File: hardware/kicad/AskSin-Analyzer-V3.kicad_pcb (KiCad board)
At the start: 4 copper layers, 118 x 46 mm, 38 parts, among them J1 Pi GPIO, J2 AVR-ISP-6, J5 OLED I2C, J6 Taster, J7 WS2812, U1 MCP1754S-3302xCB, U2 ATmega328P-AU, U3 E07-900M10S, Y1 8MHz

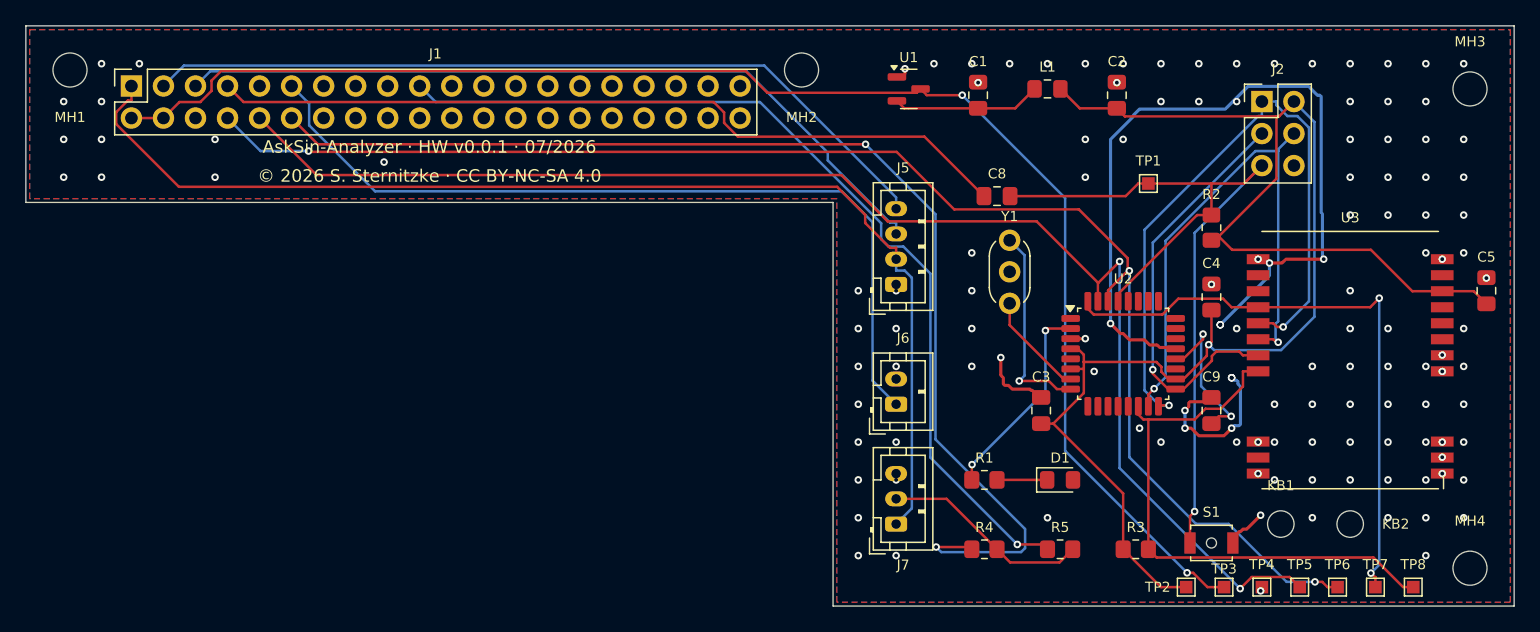
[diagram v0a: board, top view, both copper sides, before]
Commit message: Hardware v0.1.0: J1 korrigiert, Platine liegt jetzt neben dem Pi
Zwei Ursachen, ein Neuentwurf:

1. **J1 war gespiegelt.** Der Footprint wurde aus der offiziellen Vorlage
   RaspberryPi-HAT übernommen, aber ohne deren Flip auf die Unterseite.
   Die ungerade Pinreihe saß dadurch richtig, die gerade 2,54 mm auf der
   falschen Seite — aufgesteckt landet jedes Pad einen Pin daneben
   (5 V auf 3,3 V, Masse auf GPIOs). generate_pcb.py flippt J1 jetzt wie
   die Vorlage und prüft die vier Eckpads hart gegen das Pi-Raster; ein
   erneuter Fehler bricht den Lauf ab.

2. **Neue Bauform:** T-förmig statt L-förmig. Der Körper (88 × 34 mm)
   liegt parallel neben dem Pi an der Header-Seite und steht 20 mm nach
   hinten über (SD-Seite) — nicht mehr über den USB/Ethernet-Buchsen. Der
   Arm (65 × 8 mm) trägt nur die Buchse und die beiden HAT-Bohrungen.
   Funkmodul samt IPEX-Buchse sitzt im hinteren Überstand, die
   Peripheriestecker an der Frontkante.

Routing-Kette an die neue Geometrie angepasst und robuster gemacht:
- Masseflächen nur noch auf den Innenlagen; jedes SMD-Massepad bekommt
  vor dem Routen sein Stützvia (geometrisch auf Freiraum geprüft), GND
  bleibt aus dem Autorouter heraus. Damit entfallen die Splitterinseln
  und verhungerten Thermal-Speichen der Außenlagen-Füllung.
- Bohrloch-zu-Bohrloch-Wächter (räumlich indiziert) im eigenen Router
- offene Reste von Freerouting werden per A* nachgeroutet, doppelte Vias
  entfernt, alle Vias getentet
- Platinenmarkierung sucht sich ihren freien Platz selbst
- rebuild.py: baut so lange neu, bis DRC 0/0, Netzliste exakt und alle
  Massepads angebunden sind (Freerouting streut)
- finish_board.py: Absturz beim Entfernen alter Markierungstexte behoben
  (Remove -> Delete), Aufruf nie definierter Helfer entfernt

Prüfstand: ERC 0/0, DRC 0 Fehler / 0 Warnungen / 0 unverbunden,
Netzliste exakt gegen die Spezifikation, J1 gegen die HAT-Vorlage.

Co-Authored-By: Claude Fable 5 <noreply@anthropic.com>
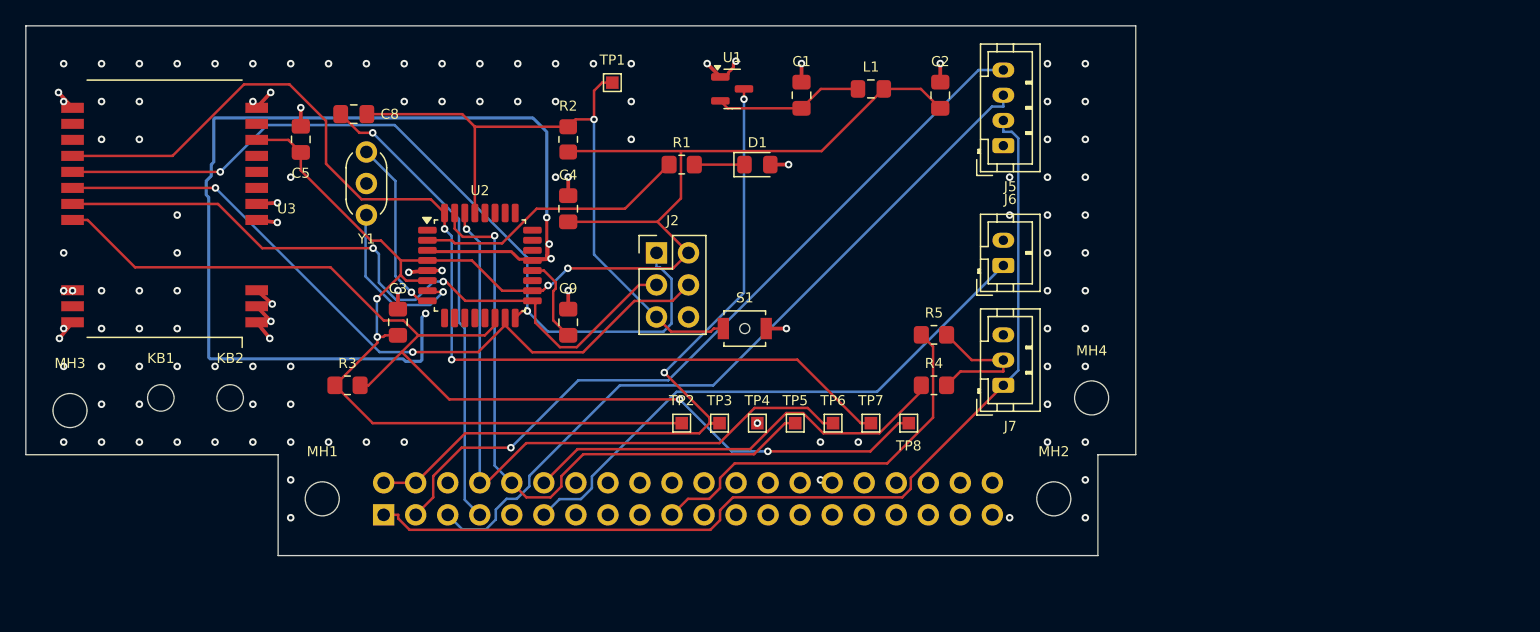
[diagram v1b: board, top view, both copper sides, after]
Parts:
- J1: moved to B.Cu
- R4: value 390 -> 390 DNP
- R5: value 0R DNP -> 0R
- moved MH3 113.9 mm to (103.5, 90.5)
- moved C5 94.8 mm to (121.8, 69.0)
- moved U3 94.8 mm to (111.0, 74.5)
- moved KB1 89.4 mm to (110.7, 89.5)
- moved KB2 89.4 mm to (116.2, 89.5)
- moved R3 63.8 mm to (125.5, 88.5)
- moved C3 51.5 mm to (129.5, 83.5)
- moved C4 51.5 mm to (143.0, 74.5)
- moved C9 51.5 mm to (143.0, 83.5)
- moved R2 51.5 mm to (143.0, 69.0)
- moved U2 51.5 mm to (136.0, 79.0)
- moved Y1 51.5 mm to (127.0, 75.0)
- moved C8 51.4 mm to (126.0, 67.0)
- moved J2 49.5 mm to (150.0, 78.0)
- moved TP1 43.2 mm to (146.5, 64.5)
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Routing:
- net UART_PI_TX: track 115.7 -> 52.9 mm, vias 3 -> 1
- net UART_328_TX: track 111.1 -> 50.7 mm, vias 2 -> 1
- net LED_PWM: track 93.9 -> 34.7 mm, vias 2 -> 0
- net +5V: track 117.6 -> 60.0 mm
- net CS: track 45.1 -> 88.8 mm, vias 0 -> 2
- net LED_SPI: track 74.3 -> 31.3 mm, vias 1 -> 0
- net GND: track 78.2 -> 116.2 mm, vias 133 -> 120
- net GDO0: track 48.3 -> 85.3 mm
- net PI_RESET_DRV: track 64.1 -> 37.0 mm, vias 0 -> 1
- net SCK: track 33.1 -> 56.5 mm, vias 1 -> 2
- net BTN: track 66.8 -> 45.2 mm
- net PI_3V3: track 93.3 -> 77.9 mm
- net MOSI: track 44.5 -> 58.8 mm
- net RESET: track 66.3 -> 53.1 mm
- net MISO: track 53.8 -> 66.0 mm
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- removed copper zone on B.Cu, net GND
- removed copper zone on F.Cu, net GND
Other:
- board size 118 x 46 mm -> 88 x 42 mm
- board text added: "AskSin-Analyzer · HW v0.1.0 · 07/2026"
- board text removed: "AskSin-Analyzer · HW v0.0.1 · 07/2026"

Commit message: J1-Adapter neu aufgebaut, Platine auf Hardware v0.2.0
**Adapter:** Die bisherige Fassung war unbrauchbar — sie setzte auf eine
Stapelbuchse, deren durchgereichte Pins mit den Stiften der zweiten
Leiste in der Höhe hätten zusammenpassen müssen. Tun sie nicht, die
Platine hätte nie aufgesessen.

Neuer Aufbau mit zwei gewöhnlichen Standardteilen: unten eine
Buchsenleiste 2x20 in exakter Pi-Geometrie (Reihen 2,23/4,77), oben eine
Stiftleiste 2x20 um 2,54 mm nach hinten versetzt (Reihen 7,31/9,85) —
genau dort erwartet die fehlerhafte Platine ihre Reihen. Jeder Pin geht
1:1 durch; ungerade Bahnen oben, gerade unten an den Pads vorbei.

Die Netze werden im Erzeuger **nach gemessener Pad-Position** vergeben
statt nach Pad-Nummer — die Verwechslung, die zum Platinenfehler geführt
hat, ist damit ausgeschlossen. verify_adapter.py prüft das fertige
Layout unabhängig gegen die offizielle KiCad-Vorlage RaspberryPi-HAT und
gegen den gefertigten Stand aus Tag hardware-v0.0.1: beide Steckbilder
decken sich mit genau einem Versatz über alle 40 Pins.
Preis: 2,54 mm Versatz nach hinten und rund 10 mm Bauhöhe.

**Platine:** Versionssprung 0.1.0 → 0.2.0, damit die neue Bauform nicht
mit der fehlerhaften Charge verwechselt wird — die Nummer steht im
Bestückungsdruck. Doku, Fertigungspaket und die 3D-Renderings im
Handbuch (Oberseite, Unterseite, Schrägansicht, Layout) auf den neuen
T-förmigen Umriss neu erzeugt.

Co-Authored-By: Claude Fable 5 <noreply@anthropic.com>
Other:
- board text added: "AskSin-Analyzer · HW v0.2.0 · 07/2026"
- board text removed: "AskSin-Analyzer · HW v0.1.0 · 07/2026"
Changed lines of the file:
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@@
 		(layer "Edge.Cuts")
 	)
-	(gr_text "© 2026 S. Sternitzke · CC BY-NC-SA 4.0"
-		(at 115.5 65.2 0)
+	(gr_text "AskSin-Analyzer · HW v0.2.0 · 07/2026"
+		(at 115.5 62.8 0)
 		(layer "B.SilkS")
 		(effects
@@
 		)
 	)
-	(gr_text "AskSin-Analyzer · HW v0.1.0 · 07/2026"
-		(at 115.5 62.8 0)
+	(gr_text "© 2026 S. Sternitzke · CC BY-NC-SA 4.0"
+		(at 115.5 65.2 0)
 		(layer "B.SilkS")
 		(effects
